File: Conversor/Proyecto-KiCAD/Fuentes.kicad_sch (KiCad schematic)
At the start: 18 parts, among them J6 Barrel_Jack_Switch, P1 SW_SPDT, P2 5V Header, P3 5V Header, P4 Jumper 2, U1 LP2985-3.3, U11 LM7805_TO252, U13 THB3-1211

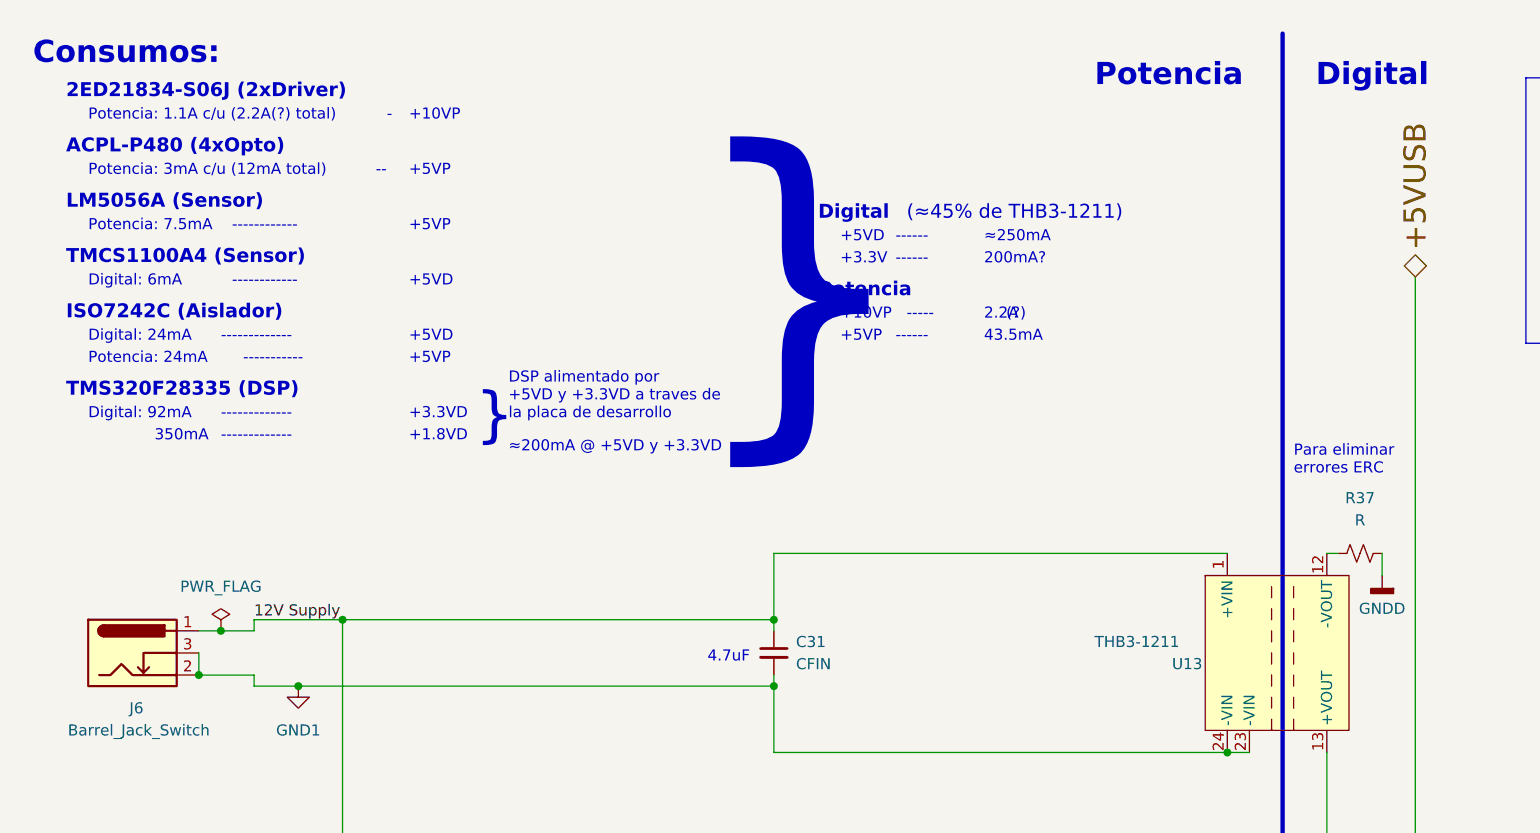
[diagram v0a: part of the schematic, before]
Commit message: Comenzar el layout de componentes de la PCB
- Todos los componentes con footprints asignados (preliminar)
- Organizados los componentes de la placa adaptadora en el esquema del
PCB (usando como guia aproximada la placa adaptadora)
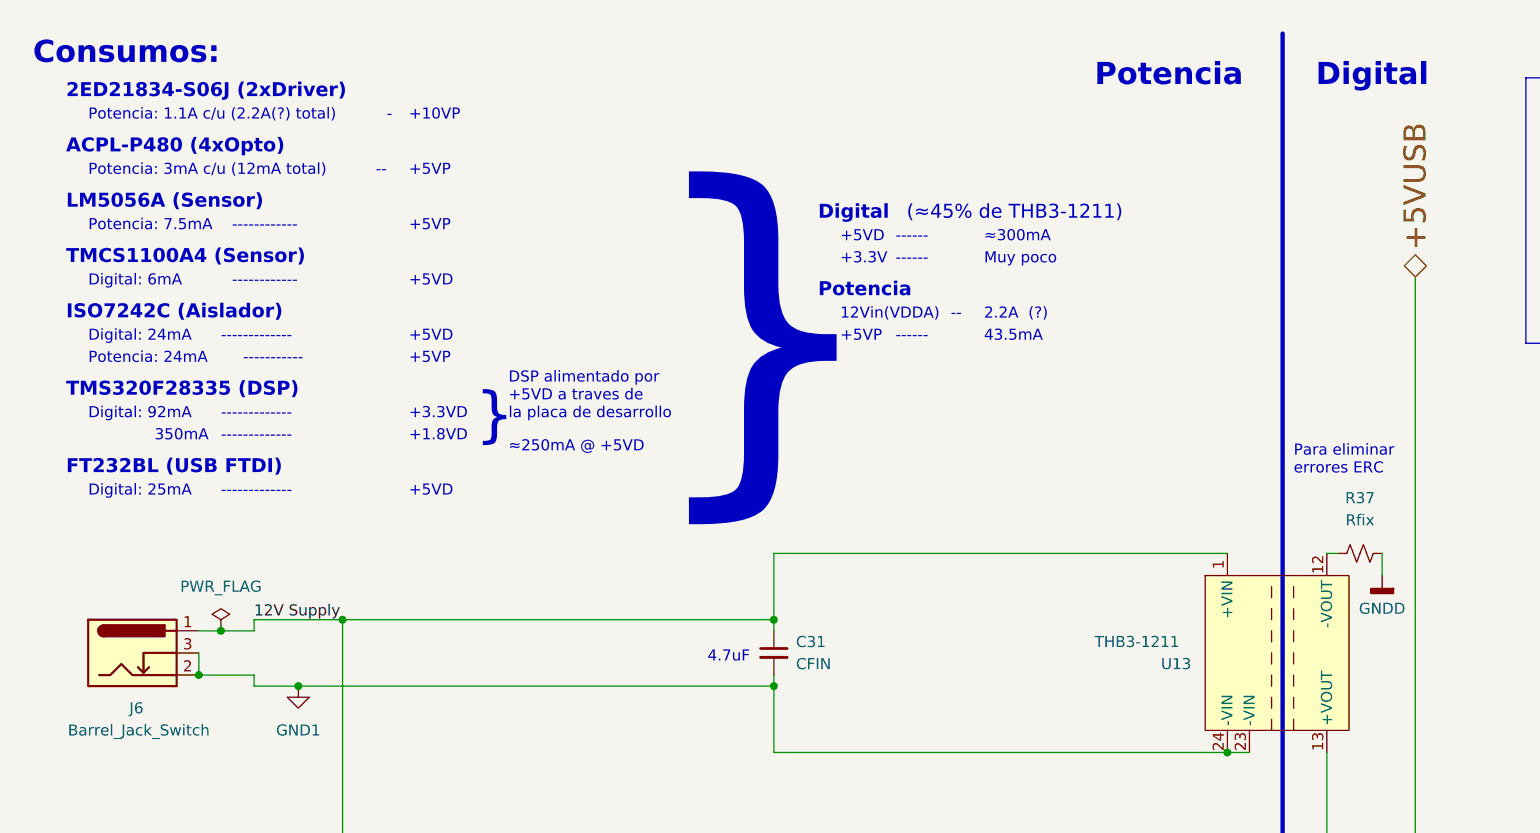
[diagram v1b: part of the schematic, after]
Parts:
- C28, C29, C30, C31, C33: footprint (none) -> Capacitor_SMD:C_1206_3216Metric_Pad1.33x1.80mm_HandSolder
- P1: footprint (none) -> Connector_PinHeader_2.54mm:PinHeader_1x03_P2.54mm_Vertical
- R10, R15, R17: footprint (none) -> Resistor_SMD:R_1206_3216Metric_Pad1.30x1.75mm_HandSolder
- R37: value R -> Rfix; footprint (none) -> Resistor_SMD:R_1206_3216Metric_Pad1.30x1.75mm_HandSolder
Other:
- note added: "12Vin(VDDA)"
- note added: "DSP alimentado por +5VD a traves de la placa de desarrollo"
- note added: "Digital: 25mA"
- note added: "FT232BL (USB FTDI)"
- note added: "Muy poco"
- note added: "≈250mA @ +5VD"
- note added: "≈300mA"
- note removed: "-----"
- note removed: "200mA?"
- note removed: "DSP alimentado por +5VD y +3.3VD a traves de la placa de desarrollo"
- note removed: "≈200mA @ +5VD y +3.3VD"
- note removed: "≈250mA"
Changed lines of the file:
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@@
   (junction (at 194.31 120.65) (diameter 0) (color 0 0 0 0)
   )
+  (junction (at 88.9 134.62) (diameter 0) (color 0 0 0 0)
+  )
+  (junction (at 78.74 125.73) (diameter 0) (color 0 0 0 0)
+  )
+  (junction (at 207.01 139.7) (diameter 0) (color 0 0 0 0)
+  )
+  (junction (at 232.41 156.21) (diameter 0) (color 0 0 0 0)
+  )
+  (junction (at 48.26 106.68) (diameter 0) (color 0 0 0 0)
+  )
+  (junction (at 43.18 87.63) (diameter 0) (color 0 0 0 0)
+  )
   (junction (at 149.86 95.25) (diameter 0) (color 0 0 0 0)
-  )
-  (junction (at 88.9 134.62) (diameter 0) (color 0 0 0 0)
-  )
-  (junction (at 78.74 125.73) (diameter 0) (color 0 0 0 0)
-  )
-  (junction (at 207.01 139.7) (diameter 0) (color 0 0 0 0)
-  )
-  (junction (at 232.41 156.21) (diameter 0) (color 0 0 0 0)
-  )
-  (junction (at 48.26 106.68) (diameter 0) (color 0 0 0 0)
-  )
-  (junction (at 43.18 87.63) (diameter 0) (color 0 0 0 0)
   )
   (junction (at 261.62 139.7) (diameter 0) (color 0 0 0 0)
@@
     (stroke (width 0) (type default) (color 0 0 0 0))
   )
+  (wire (pts (xy 149.86 95.25) (xy 152.4 95.25))
+    (stroke (width 0) (type default) (color 0 0 0 0))
+  )
   (wire (pts (xy 160.02 152.4) (xy 173.99 152.4))
     (stroke (width 0) (type default) (color 0 0 0 0))
@@
   )
   (polyline (pts (xy 184.15 48.26) (xy 224.79 48.26))
-    (stroke (width 0) (type default) (color 0 0 0 0))
-  )
-  (wire (pts (xy 149.86 95.25) (xy 152.4 95.25))
     (stroke (width 0) (type default) (color 0 0 0 0))
   )
@@
     (effects (font (size 1.27 1.27)) (justify left bottom))
   )
-  (text "(?)" (at 124.46 45.72 0)
+  (text "(?)" (at 127 45.72 0)
     (effects (font (size 1.27 1.27)) (justify left bottom))
   )
@@
     (effects (font (size 1.27 1.27)) (justify left bottom))
   )
-  (text "-----" (at 113.03 45.72 0)
+  (text "--" (at 118.11 45.72 0)
     (effects (font (size 1.27 1.27)) (justify left bottom))
   )
@@
     (effects (font (size 1.27 1.27)) (justify left bottom))
   )
+  (text "+5VD" (at 55.88 66.04 0)
+    (effects (font (size 1.27 1.27)) (justify left bottom))
+  )
+  (text "Digital: 25mA" (at 19.05 66.04 0)
+    (effects (font (size 1.27 1.27)) (justify left bottom))
+  )
   (text "Digital" (at 161.29 195.58 0)
     (effects (font (size 2.54 2.54) (thickness 0.508) bold) (justify left bottom))
@@
     (effects (font (size 1.27 1.27)) (justify left bottom))
   )
-  (text "≈250mA" (at 121.92 36.83 0)
+  (text "≈300mA" (at 121.92 36.83 0)
     (effects (font (size 1.27 1.27)) (justify left bottom))
   )
@@
     (effects (font (size 1.27 1.27)) (justify left bottom))
   )
-  (text "+10VP" (at 105.41 45.72 0)
+  (text "12Vin(VDDA)" (at 105.41 45.72 0)
     (effects (font (size 1.27 1.27)) (justify left bottom))
   )
@@
     (effects (font (size 1.6 1.6) (thickness 0.32) bold) (justify left bottom))
   )
-  (text "200mA?" (at 121.92 39.37 0)
+  (text "Muy poco" (at 121.92 39.37 0)
     (effects (font (size 1.27 1.27)) (justify left bottom))
   )
@@
     (effects (font (size 1.27 1.27)) (justify left bottom))
   )
-  (text "≈200mA @ +5VD y +3.3VD" (at 67.31 60.96 0)
+  (text "≈250mA @ +5VD" (at 67.31 60.96 0)
+    (effects (font (size 1.27 1.27)) (justify left bottom))
+  )
+  (text "-------------" (at 34.29 66.04 0)
     (effects (font (size 1.27 1.27)) (justify left bottom))
   )
@@
     (effects (font (size 1.27 1.27)) (justify left bottom))
   )
-  (text "}" (at 87.63 59.69 0)
-    (effects (font (size 30 30)) (justify left bottom))
+  (text "}" (at 82.55 66.04 0)
+    (effects (font (size 32 32)) (justify left bottom))
   )
   (text "2ED21834-S06J (2xDriver)" (at 16.51 20.32 0)
@@
     (effects (font (size 2.54 2.54) (thickness 0.508) bold) (justify left bottom))
   )
-  (text "DSP alimentado por\n+5VD y +3.3VD a traves de\nla placa de desarrollo"
+  (text "DSP alimentado por\n+5VD a traves de\nla placa de desarrollo"
     (at 67.31 57.15 0)
     (effects (font (size 1.27 1.27)) (justify left bottom))
@@
     (effects (font (size 1.27 1.27)) (justify left bottom))
   )
+  (text "FT232BL (USB FTDI)" (at 16.51 63.5 0)
+    (effects (font (size 1.6 1.6) (thickness 0.32) bold) (justify left bottom))
+  )
   (text "+5VP" (at 105.41 48.26 0)
     (effects (font (size 1.27 1.27)) (justify left bottom))
@@
       (effects (font (size 1.27 1.27)) (justify left))
     )
-    (property "Footprint" "" (id 2) (at 99.06 130.81 0)
+    (property "Footprint" "Capacitor_SMD:C_1206_3216Metric_Pad1.33x1.80mm_HandSolder" (id 2) (at 99.06 130.81 0)
       (effects (font (size 1.27 1.27)) hide)
     )
@@
     (property "Reference" "R17" (id 0) (at 132.08 160.02 90))
     (property "Value" "0" (id 1) (at 132.08 162.56 90))
-    (property "Footprint" "" (id 2) (at 132.334 156.464 90)
+    (property "Footprint" "Resistor_SMD:R_1206_3216Metric_Pad1.30x1.75mm_HandSolder" (id 2) (at 132.334 156.464 90)
       (effects (font (size 1.27 1.27)) hide)
     )
@@
       (effects (font (size 1.27 1.27)) (justify left))
     )
-    (property "Footprint" "" (id 2) (at 97.79 83.82 0)
+    (property "Footprint" "Capacitor_SMD:C_1206_3216Metric_Pad1.33x1.80mm_HandSolder" (id 2) (at 97.79 83.82 0)
       (effects (font (size 1.27 1.27)) hide)
     )
@@
   (symbol (lib_id "Componentes proyecto:THB3-1211") (at 153.67 83.82 90) (mirror x) (unit 1)
     (in_bom yes) (on_board yes)
-    (property "Reference" "U13" (id 0) (at 143.51 85.09 90)
+    (property "Reference" "U13" (id 0) (at 142.24 85.09 90)
       (effects (font (size 1.27 1.27)) (justify right))
     )
@@
     (property "Reference" "R10" (id 0) (at 156.21 142.24 90))
     (property "Value" "0" (id 1) (at 156.21 144.78 90))
-    (property "Footprint" "" (id 2) (at 156.464 146.304 90)
+    (property "Footprint" "Resistor_SMD:R_1206_3216Metric_Pad1.30x1.75mm_HandSolder" (id 2) (at 156.464 146.304 90)
       (effects (font (size 1.27 1.27)) hide)
     )
@@
     (property "Reference" "P1" (id 0) (at 187.96 113.03 0))
     (property "Value" "SW_SPDT" (id 1) (at 187.96 115.57 0))
-    (property "Footprint" "" (id 2) (at 187.96 120.65 0)
+    (property "Footprint" "Connector_PinHeader_2.54mm:PinHeader_1x03_P2.54mm_Vertical" (id 2) (at 187.96 120.65 0)
       (effects (font (size 1.27 1.27)) hide)
     )
@@
     (in_bom yes) (on_board yes) (fields_autoplaced)
     (property "Reference" "R37" (id 0) (at 165.1 66.04 90))
-    (property "Value" "R" (id 1) (at 165.1 68.58 90))
-    (property "Footprint" "" (id 2) (at 165.1 72.39 0)
+    (property "Value" "Rfix" (id 1) (at 165.1 68.58 90))
+    (property "Footprint" "Resistor_SMD:R_1206_3216Metric_Pad1.30x1.75mm_HandSolder" (id 2) (at 165.1 72.39 0)
       (effects (font (size 1.27 1.27)) hide)
     )
@@
       (effects (font (size 1.27 1.27)) (justify left))
     )
-    (property "Footprint" "" (id 2) (at 261.62 151.13 0)
+    (property "Footprint" "Capacitor_SMD:C_1206_3216Metric_Pad1.33x1.80mm_HandSolder" (id 2) (at 261.62 151.13 0)
       (effects (font (size 1.27 1.27)) hide)
     )
@@
       (effects (font (size 1.27 1.27)) (justify left))
     )
-    (property "Footprint" "" (id 2) (at 207.01 147.32 0)
+    (property "Footprint" "Capacitor_SMD:C_1206_3216Metric_Pad1.33x1.80mm_HandSolder" (id 2) (at 207.01 147.32 0)
       (effects (font (size 1.27 1.27)) hide)
     )
@@
       (effects (font (size 1.27 1.27)) (justify left))
     )
-    (property "Footprint" "" (id 2) (at 78.74 130.81 0)
+    (property "Footprint" "Capacitor_SMD:C_1206_3216Metric_Pad1.33x1.80mm_HandSolder" (id 2) (at 78.74 130.81 0)
       (effects (font (size 1.27 1.27)) hide)
     )
@@
     (property "Reference" "R15" (id 0) (at 156.21 149.86 90))
     (property "Value" "0" (id 1) (at 156.21 154.94 90))
-    (property "Footprint" "" (id 2) (at 156.464 151.384 90)
-      (effects (font (size 1.27 1.27)) hide)
-    )
+    (property "Footprint" "Resistor_SMD:R_1206_3216Metric_Pad1.30x1.75mm_HandSolder" (id 2) (at 156.464 151.384 90)
+      (effects (font (size 1.27 1.27)) hide)
+    )

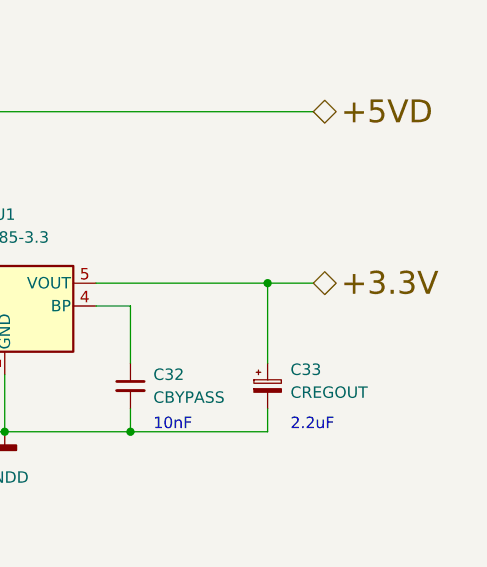
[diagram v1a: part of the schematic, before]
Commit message: Reempezar el ordenado de componentes del PCB
- Intentar copiar mas a la placa adaptadora en la parte del DSP (digital)
  - Algunas cosas (como los headers y la parte de USB) se movieron para hacer entrar mejor las cosas
- Layout bastante completo
- Agregados algunos modelos 3D faltantes
Por hacer:
  - Mover y reorganizar la parte del LM5056, porque tiene una pata que va al secundario, y ahora esta muy lejos del area de GND2
  - Ver como reorganizar un poco para que no queden esquinas vacias
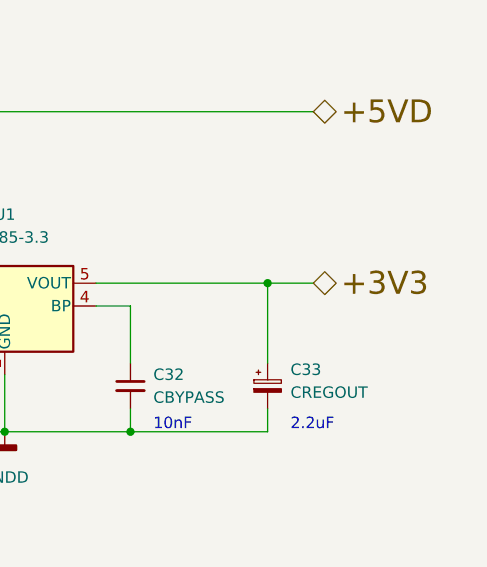
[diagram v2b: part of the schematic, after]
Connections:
- net +3.3V renamed +3V3
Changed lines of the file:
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@@
     (effects (font (size 2.54 2.54)) (justify left))
   )
-  (hierarchical_label "+3.3V" (shape bidirectional) (at 266.7 139.7 0)
+  (hierarchical_label "+3V3" (shape bidirectional) (at 266.7 139.7 0)
     (effects (font (size 2.54 2.54)) (justify left))
   )

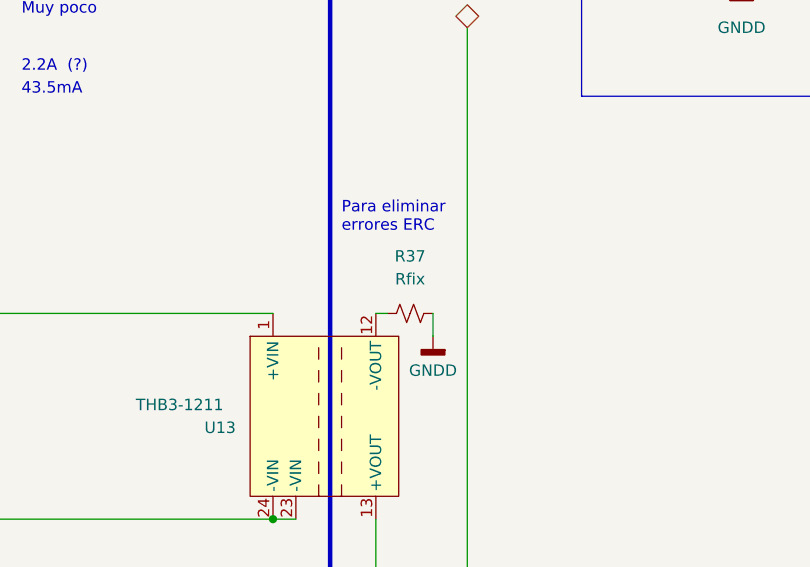
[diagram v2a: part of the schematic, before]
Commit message: Terminar la parte digital de la PCB (incluidas las pistas)
- Hay que ver si la clearance de 0.254mm para el plano de GNDD esta bien
- Cambiar la footprint del FTDI por la version correcta
- Borrar R37, R38 y R39 (usadas para corregir errores del ERC)
Por hacer:
  - Terminar las otras dos partes de la placa
  - Consultar si esta bien lo que hice hasta ahora
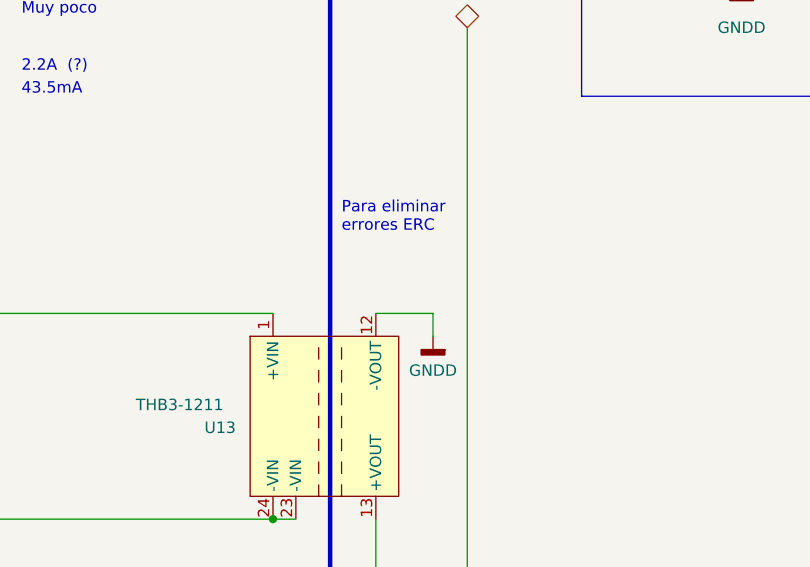
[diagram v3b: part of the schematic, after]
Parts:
- removed R37: Rfix, Resistor_SMD:R_1206_3216Metric_Pad1.30x1.75mm_HandSolder, symbol Device:R_Small_US
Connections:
- net GNDD: now also U13.12 (-VOUT)
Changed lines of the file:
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@@
     (stroke (width 0) (type default) (color 0 0 0 0))
   )
-  (wire (pts (xy 161.29 72.39) (xy 162.56 72.39))
+  (wire (pts (xy 161.29 72.39) (xy 167.64 72.39))
     (stroke (width 0) (type default) (color 0 0 0 0))
   )
@@
     (pin "3")
   )
-  (symbol (lib_id "Device:R_Small_US") (at 165.1 72.39 90) (unit 1)
-    (in_bom yes) (on_board yes) (fields_autoplaced)
-    (property "Reference" "R37" (id 0) (at 165.1 66.04 90))
-    (property "Value" "Rfix" (id 1) (at 165.1 68.58 90))
-    (property "Footprint" "Resistor_SMD:R_1206_3216Metric_Pad1.30x1.75mm_HandSolder" (id 2) (at 165.1 72.39 0)
-      (effects (font (size 1.27 1.27)) hide)
-    )
-    (property "Datasheet" "~" (id 3) (at 165.1 72.39 0)
-      (effects (font (size 1.27 1.27)) hide)
-    )
-    (pin "1")
-    (pin "2")
-  )
   (symbol (lib_id "Device:C_Polarized_Small") (at 261.62 151.13 0) (unit 1)
